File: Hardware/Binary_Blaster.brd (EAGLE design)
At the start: 86.4 x 68.6 mm, 26 parts

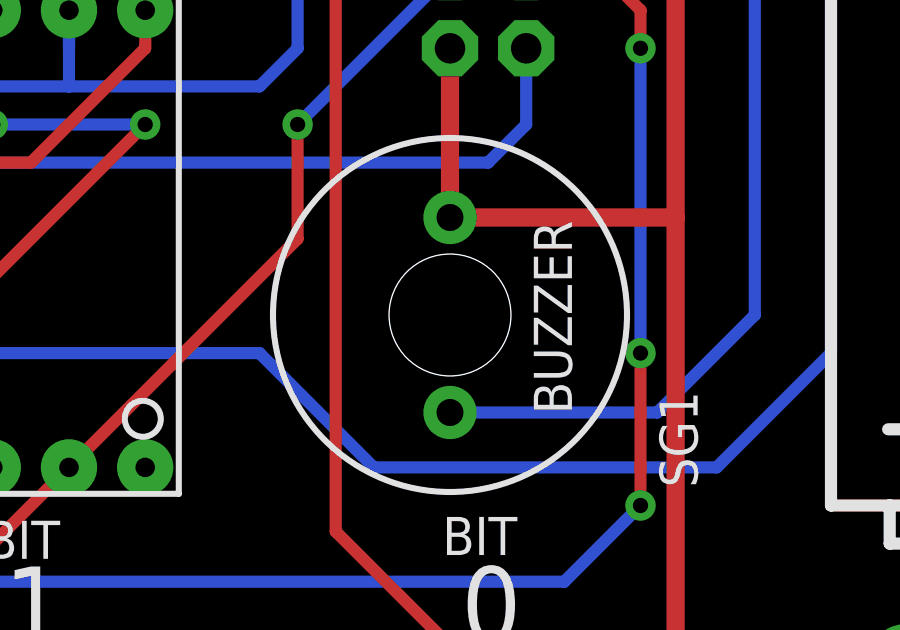
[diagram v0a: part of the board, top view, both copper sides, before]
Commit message: replaced devices with Prod_ID versions
Also included gitignore and removed version number from board/sch file
names.
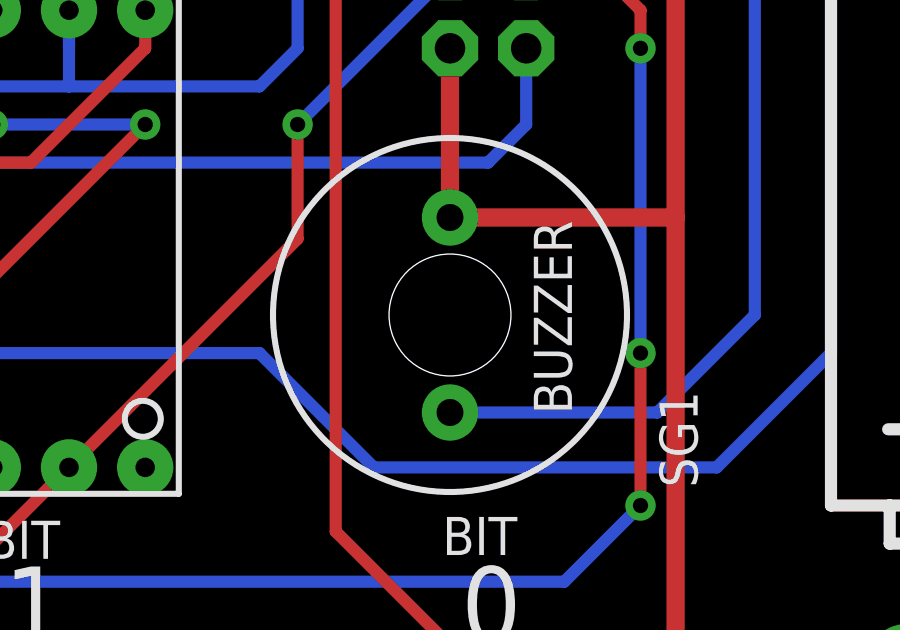
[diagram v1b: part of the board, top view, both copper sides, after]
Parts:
- BAT1, BAT2: device SparkFun:BATTERY-AA-KIT -> SparkFun-Electromechanical:BATTERY-AA-KIT
- C1, C2: device SparkFun:CAP-PTH-SMALL-KIT -> SparkFun-Capacitors:CAP-PTH-SMALL-KIT
- R1: device SparkFun:AXIAL-0.3-KIT -> SparkFun-Resistors:AXIAL-0.3-KIT
- S1, S2: device SparkFun:SWITCH-SPDT_KIT -> SparkFun-Electromechanical:SWITCH-SPDT_KIT
- SG1: device SparkFun:BUZZER-12MM-KIT -> SparkFun-Electromechanical:BUZZER-12MM-KIT
- moved C1 1.27 mm to (66.0, 48.3)
- moved C2 1.27 mm to (20.3, 48.3)
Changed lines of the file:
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@@
 <layer number="27" name="tValues" color="7" fill="1" visible="no" active="yes"/>
 <layer number="28" name="bValues" color="7" fill="1" visible="no" active="yes"/>
-<layer number="29" name="tStop" color="4" fill="3" visible="no" active="yes"/>
-<layer number="30" name="bStop" color="1" fill="6" visible="no" active="yes"/>
+<layer number="29" name="tStop" color="4" fill="3" visible="yes" active="yes"/>
+<layer number="30" name="bStop" color="1" fill="6" visible="yes" active="yes"/>
 <layer number="31" name="tCream" color="7" fill="4" visible="no" active="yes"/>
 <layer number="32" name="bCream" color="7" fill="5" visible="no" active="yes"/>
@@
 </autorouter>
 <elements>
-<element name="S1" library="SparkFun" package="SWITCH-SPDT_KIT" value="Power" x="21.59" y="63.5" rot="R270"/>
-<element name="S2" library="SparkFun" package="SWITCH-SPDT_KIT" value="" x="64.77" y="63.5" rot="R90"/>
-<element name="BAT1" library="SparkFun" package="BATTERY-AA-KIT" value="AA" x="6.35" y="34.29" rot="R270"/>
-<element name="SG1" library="SparkFun" package="BUZZER-12MM-KIT" value="BUZZER" x="64.77" y="27.94" smashed="yes" rot="R270">
+<element name="S1" library="SparkFun-Electromechanical" package="SWITCH-SPDT_KIT" value="Power" x="21.59" y="63.5" rot="R270">
+<attribute name="PROD_ID" value="SWCH-08261" x="21.59" y="63.5" size="1.778" layer="27" rot="R270" display="off"/>
+</element>
+<element name="S2" library="SparkFun-Electromechanical" package="SWITCH-SPDT_KIT" value="" x="64.77" y="63.5" rot="R90">
+<attribute name="PROD_ID" value="SWCH-08261" x="64.77" y="63.5" size="1.778" layer="27" rot="R90" display="off"/>
+</element>
+<element name="BAT1" library="SparkFun-Electromechanical" package="BATTERY-AA-KIT" value="AA" x="6.35" y="34.29" rot="R270">
+<attribute name="PROD_ID" value="BATT-08316" x="6.35" y="34.29" size="1.778" layer="27" rot="R270" display="off"/>
+</element>
+<element name="SG1" library="SparkFun-Electromechanical" package="BUZZER-12MM-KIT" value="BUZZER" x="64.77" y="27.94" smashed="yes" rot="R270">
 <attribute name="NAME" x="71.755" y="25.4" size="1.27" layer="25" ratio="10" rot="R270"/>
+<attribute name="PROD_ID" value="COMP-08253" x="64.77" y="27.94" size="1.778" layer="27" rot="R270" display="off"/>
 </element>
 <element name="JP3" library="SparkFun" package="2X3-NS" value="" x="66.04" y="39.37" smashed="yes" rot="MR270"/>
-<element name="C2" library="SparkFun" package="CAP-PTH-SMALL-KIT" value="0.1uF" x="20.32" y="49.53" smashed="yes" rot="R270"/>
+<element name="C2" library="SparkFun-Capacitors" package="CAP-PTH-SMALL-KIT" value="0.1uF" x="20.32" y="48.26" smashed="yes" rot="R270">
+<attribute name="PROD_ID" value="CAP-08370" x="20.32" y="48.26" size="1.778" layer="27" rot="R270" display="off"/>
+</element>
 <element name="JP1" library="unclepetes" package="1X06-NOSILK" value="Serial" x="1.27" y="40.64" smashed="yes" rot="MR270">
 <attribute name="NAME" x="-0.5588" y="41.9862" size="1.27" layer="26" ratio="10" rot="MR270"/>
 </element>
-<element name="R1" library="SparkFun" package="AXIAL-0.3-KIT" value="10K" x="21.59" y="36.83" smashed="yes">
+<element name="R1" library="SparkFun-Resistors" package="AXIAL-0.3-KIT" value="10K" x="21.59" y="36.83" smashed="yes">
 <attribute name="NAME" x="19.05" y="38.1" size="0.4064" layer="25"/>
 <attribute name="VALUE" x="19.812" y="36.195" size="1.27" layer="21" ratio="15"/>
+<attribute name="PROD_ID" value="RES-08375" x="21.59" y="36.83" size="1.778" layer="27" display="off"/>
 </element>
-<element name="BAT2" library="SparkFun" package="BATTERY-AA-KIT" value="AA" x="80.01" y="34.29" rot="R90"/>
-<element name="C1" library="SparkFun" package="CAP-PTH-SMALL-KIT" value="0.1uF" x="66.04" y="49.53" rot="R270"/>
+<element name="BAT2" library="SparkFun-Electromechanical" package="BATTERY-AA-KIT" value="AA" x="80.01" y="34.29" rot="R90">
+<attribute name="PROD_ID" value="BATT-08316" x="80.01" y="34.29" size="1.778" layer="27" rot="R90" display="off"/>
+</element>
+<element name="C1" library="SparkFun-Capacitors" package="CAP-PTH-SMALL-KIT" value="0.1uF" x="66.04" y="48.26" rot="R270">
+<attribute name="PROD_ID" value="CAP-08370" x="66.04" y="48.26" size="1.778" layer="27" rot="R270" display="off"/>
+</element>
 <element name="JP2" library="SparkFun" package="STAND-OFF" value="STAND-OFF" x="82.55" y="3.81"/>
 <element name="JP5" library="SparkFun" package="STAND-OFF" value="STAND-OFF" x="3.81" y="64.77"/>
@@
 </signal>
 </signals>
-<errors>
-</errors>
 </board>
 </drawing>

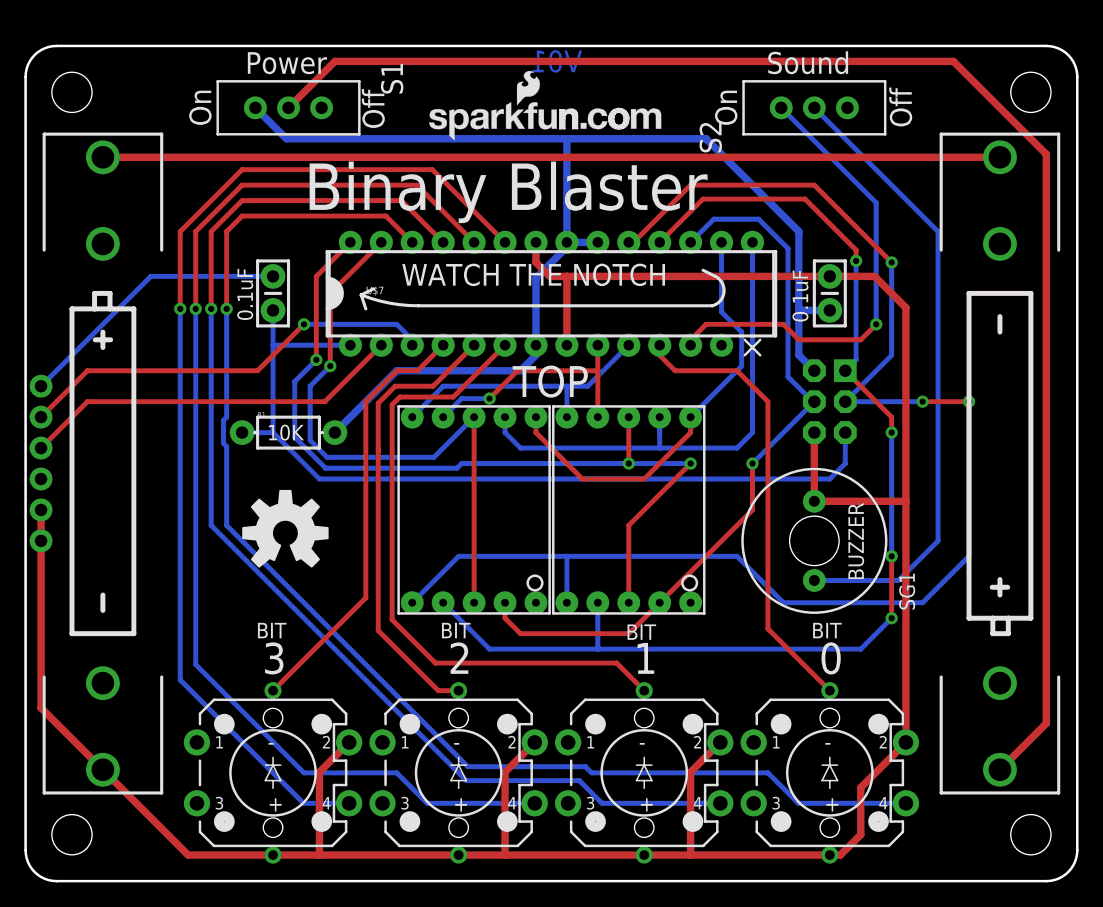
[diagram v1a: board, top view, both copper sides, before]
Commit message: Firmware and "v02" of hardware
v02: changed to "EZ" packages on display and leds, corrected silk on led
package. Moved to larger display (the we carry in house).
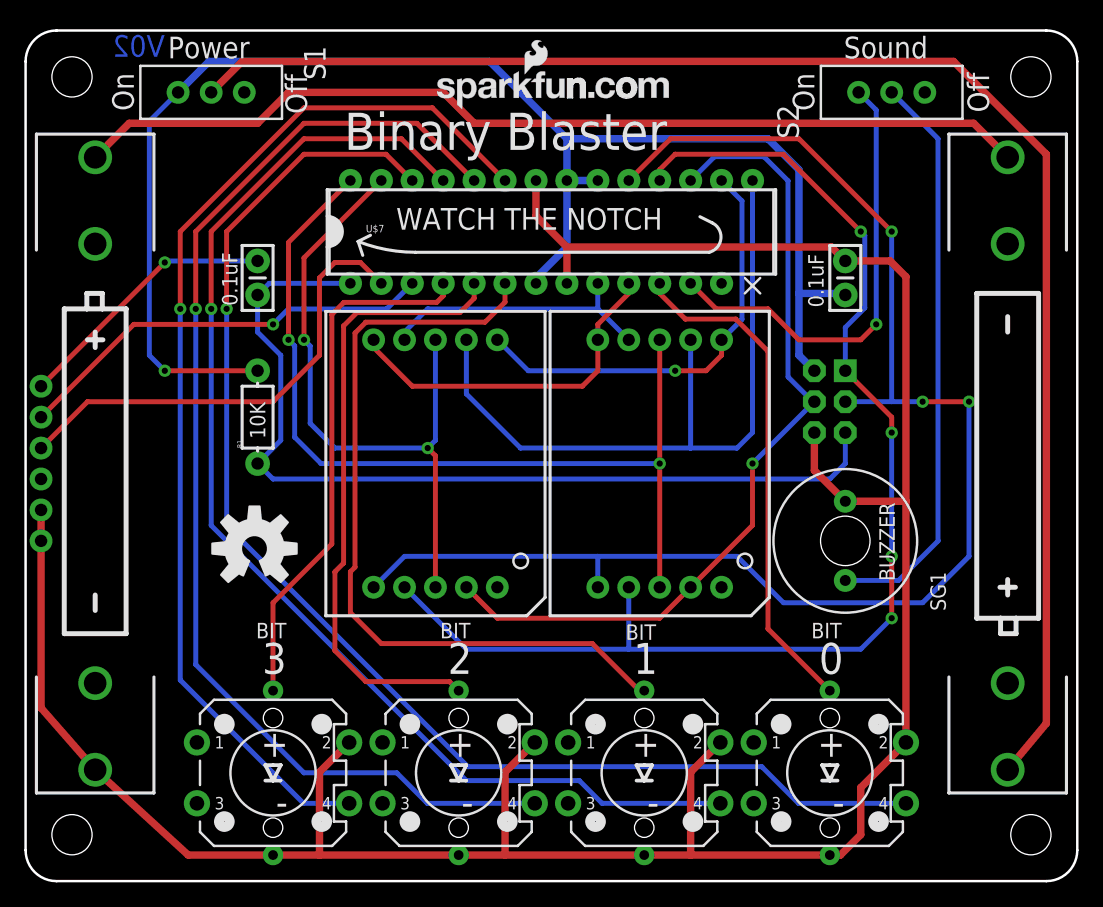
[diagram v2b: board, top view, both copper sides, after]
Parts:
- removed U$4, U$5: (no value), SparkFun-Displays:7-SEGMENT-DISPLAY
- added U$1, U$6: 7-SEGMENT-DISPLAY-1"-REDEZ, SparkFun-Displays:7-SEGMENT-1"PTH-EZ
- S3, S4, S5, S6: value (none) -> SWITCH-MOMENTARY-LEDEZ; device SparkFun-Electromechanical:TACTILE-PTH-LED-12MM -> SparkFun-Electromechanical:TACTILE-PTH-LED-12MM-EZ
- moved S2 6.48 mm to (71.1, 64.8)
- moved S1 6.48 mm to (15.2, 64.8)
- moved U$7 5.08 mm to (43.2, 53.3)
- moved R1 2.84 mm to (19.1, 38.1), turned to 90 degrees
- moved U$2 2.84 mm to (18.8, 27.3)
- moved LOGO1 2.62 mm to (33.8, 63.4)
- moved SG1 2.54 mm to (67.3, 27.9)
- moved C2 1.80 mm to (19.1, 49.5)
- moved C1 1.80 mm to (67.3, 49.5)
- moved JP5 1.27 mm to (3.81, 66.0)
- moved JP6 1.27 mm to (82.5, 66.0)
- moved BAT1 0.63 mm to (5.71, 34.3)
- moved BAT2 0.63 mm to (80.6, 34.3)
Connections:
- net A: now also U$1.7, U$6.7; no longer U$4.7, U$5.7
- net B: now also U$1.6, U$6.6; no longer U$4.6, U$5.6
- net C: now also U$1.4, U$6.4; no longer U$4.4, U$5.4
- net D: now also U$1.2, U$6.2; no longer U$4.2, U$5.2
- net D1: now also U$1.3, U$1.8; no longer U$5.3, U$5.8
- net D2: now also U$6.3, U$6.8; no longer U$4.3, U$4.8
- net E: now also U$1.1, U$6.1; no longer U$4.1, U$5.1
- net F: now also U$1.9, U$6.9; no longer U$4.9, U$5.9
- net G: now also U$1.10, U$6.10; no longer U$4.10, U$5.10
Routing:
- net 3.3V: track 103.9 -> 124.1 mm, vias 0 -> 1
- net A: track 42.1 -> 59.9 mm
- net LED1: track 37.2 -> 51.4 mm
- net LED2: track 52.1 -> 65.4 mm
- net LED0: track 35.2 -> 43.7 mm
- net D: track 94.8 -> 102.9 mm
- net C: track 60.6 -> 68.7 mm
- net RX-I: track 31.4 -> 38.7 mm
- net G: track 22.8 -> 29.1 mm
- net N$4: track 73.7 -> 79.3 mm
- net D2: track 69.0 -> 74.6 mm, vias 3 -> 2
- net N$2: track 119.1 -> 124.5 mm
- net D1: track 49.3 -> 54.1 mm, vias 1 -> 2
- net RESET: track 70.6 -> 75.3 mm
- net LED3: track 37.1 -> 41.7 mm
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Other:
- board size 86.4 x 68.6 mm -> 86.4 x 69.8 mm
- board text added: "V02"
- board text removed: "TOP"
- board text removed: "V01"
